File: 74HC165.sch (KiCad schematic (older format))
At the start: 6 parts, among them J10 Conn_01x04, J9 Conn_01x04, U1 74HC165

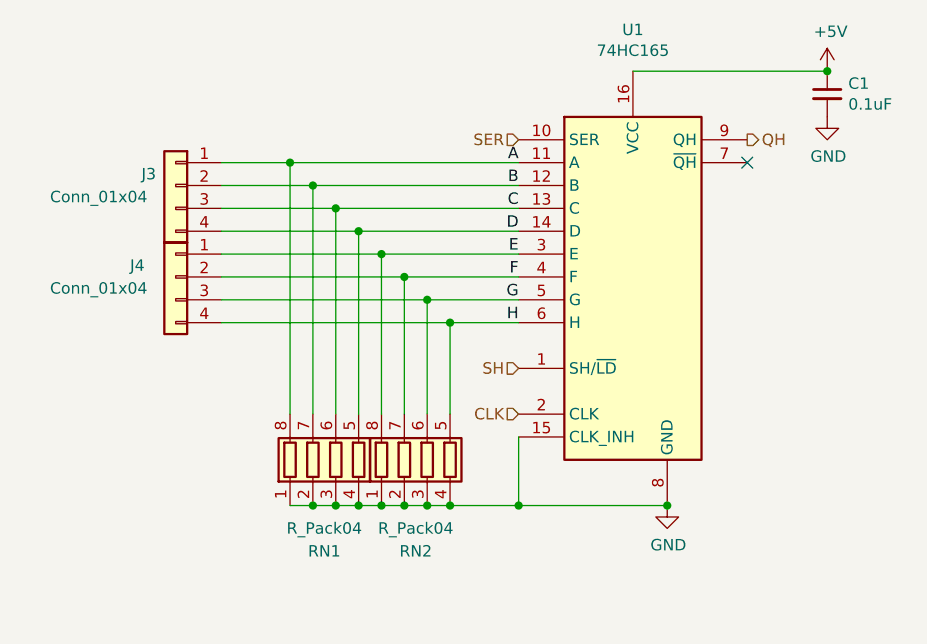
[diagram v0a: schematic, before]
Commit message: Add GND to each header, remove daisy chain
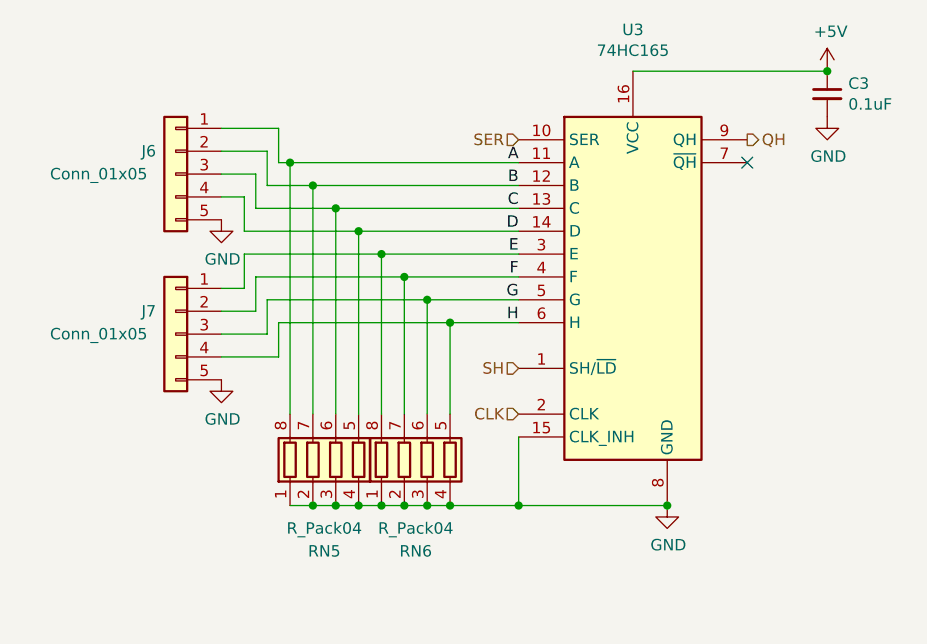
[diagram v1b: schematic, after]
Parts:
- removed J10, J9: Conn_01x04, Connector_JST:JST_XH_B4B-XH-AM_1x04_P2.50mm_Vertical, symbol Connector_Generic:Conn_01x04
- added J2, J3: Conn_01x05, Connector_JST:JST_XH_B5B-XH-A_1x05_P2.50mm_Vertical, symbol Connector_Generic:Conn_01x05
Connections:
- net A: now also J2.1 (Pin_1)
- net B: now also J2.2 (Pin_2)
- net C: now also J2.3 (Pin_3)
- net D: now also J2.4 (Pin_4)
- net E: now also J3.1 (Pin_1)
- net F: now also J3.2 (Pin_2)
- net G: now also J3.3 (Pin_3)
- net GND: now also J2.5 (Pin_5), J3.5 (Pin_5)
- net H: now also J3.4 (Pin_4)
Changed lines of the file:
@@
 $Descr A4 11693 8268
 encoding utf-8
-Sheet 2 5
+Sheet 4 5
 Title ""
 Date "%%date%%"
@@
 AR Path="/61DDC3C8/61DD4B9D" Ref="U3"  Part="1"
 AR Path="/61DDC5F2/61DD4B9D" Ref="U4"  Part="1"
-F 0 "U1" H 3350 2931 50  0000 C CNN
+F 0 "U3" H 3350 2931 50  0000 C CNN
 F 1 "74HC165" H 3350 2840 50  0000 C CNN
 F 2 "Package_SO:TSSOP-16_4.4x5mm_P0.65mm" H 3350 1850 50  0001 C CNN
@@
 AR Path="/61DDC3C8/61DD4BA3" Ref="C3"  Part="1"
 AR Path="/61DDC5F2/61DD4BA3" Ref="C4"  Part="1"
-F 0 "C1" H 4292 1096 50  0000 L CNN
+F 0 "C3" H 4292 1096 50  0000 L CNN
 F 1 "0.1uF" H 4292 1005 50  0000 L CNN
 F 2 "Capacitor_SMD:C_0805_2012Metric" H 4200 1050 50  0001 C CNN
@@
 	2850 2850 3500 2850
 Wire Wire Line
-	1550 1950 2450 1950
-Wire Wire Line
-	1550 2050 2550 2050
-Wire Wire Line
 	2550 2450 2550 2050
-Connection ~ 2550 2050
 Wire Wire Line
 	2550 2050 2850 2050
 Wire Wire Line
-	1550 1350 1850 1350
-Wire Wire Line
-	1550 1450 1950 1450
-Wire Wire Line
-	1550 1550 2050 1550
-Wire Wire Line
-	1550 1650 2150 1650
-Wire Wire Line
-	1550 1750 2250 1750
-Wire Wire Line
-	1550 1850 2350 1850
-Wire Wire Line
 	2450 2450 2450 1950
-Connection ~ 2450 1950
 Wire Wire Line
 	2450 1950 2850 1950
 Wire Wire Line
 	2350 2450 2350 1850
-Connection ~ 2350 1850
 Wire Wire Line
 	2350 1850 2850 1850
 Wire Wire Line
 	2250 2450 2250 1750
-Connection ~ 2250 1750
 Wire Wire Line
 	2250 1750 2850 1750
 Wire Wire Line
 	2150 2450 2150 1650
-Connection ~ 2150 1650
 Wire Wire Line
 	2150 1650 2850 1650
 Wire Wire Line
 	2050 2450 2050 1550
-Connection ~ 2050 1550
 Wire Wire Line
 	2050 1550 2850 1550
 Wire Wire Line
 	1950 2450 1950 1450
-Connection ~ 1950 1450
 Wire Wire Line
 	1950 1450 2850 1450
 Wire Wire Line
 	1850 2450 1850 1350
-Connection ~ 1850 1350
 Wire Wire Line
 	1850 1350 2850 1350
@@
 AR Path="/61DD4BEE" Ref="#PWR?"  Part="1"
 AR Path="/61DCCBDC/61DD4BEE" Ref="#PWR07"  Part="1"
-AR Path="/61DDC172/61DD4BEE" Ref="#PWR010"  Part="1"
-AR Path="/61DDC3C8/61DD4BEE" Ref="#PWR013"  Part="1"
-AR Path="/61DDC5F2/61DD4BEE" Ref="#PWR016"  Part="1"
-F 0 "#PWR07" H 3500 2600 50  0001 C CNN
+AR Path="/61DDC172/61DD4BEE" Ref="#PWR012"  Part="1"
+AR Path="/61DDC3C8/61DD4BEE" Ref="#PWR017"  Part="1"
+AR Path="/61DDC5F2/61DD4BEE" Ref="#PWR022"  Part="1"
+F 0 "#PWR017" H 3500 2600 50  0001 C CNN
 F 1 "GND" H 3505 2677 50  0000 C CNN
 F 2 "" H 3500 2850 50  0001 C CNN
@@
 P 4200 950
 AR Path="/61DD4BF6" Ref="#PWR?"  Part="1"
-AR Path="/61DCCBDC/61DD4BF6" Ref="#PWR05"  Part="1"
+AR Path="/61DCCBDC/61DD4BF6" Ref="#PWR03"  Part="1"
 AR Path="/61DDC172/61DD4BF6" Ref="#PWR08"  Part="1"
-AR Path="/61DDC3C8/61DD4BF6" Ref="#PWR011"  Part="1"
-AR Path="/61DDC5F2/61DD4BF6" Ref="#PWR014"  Part="1"
-F 0 "#PWR05" H 4200 800 50  0001 C CNN
+AR Path="/61DDC3C8/61DD4BF6" Ref="#PWR013"  Part="1"
+AR Path="/61DDC5F2/61DD4BF6" Ref="#PWR018"  Part="1"
+F 0 "#PWR013" H 4200 800 50  0001 C CNN
 F 1 "+5V" H 4215 1123 50  0000 C CNN
 F 2 "" H 4200 950 50  0001 C CNN
@@
 P 4200 1150
 AR Path="/61DD4BFD" Ref="#PWR?"  Part="1"
-AR Path="/61DCCBDC/61DD4BFD" Ref="#PWR06"  Part="1"
+AR Path="/61DCCBDC/61DD4BFD" Ref="#PWR04"  Part="1"
 AR Path="/61DDC172/61DD4BFD" Ref="#PWR09"  Part="1"
-AR Path="/61DDC3C8/61DD4BFD" Ref="#PWR012"  Part="1"
-AR Path="/61DDC5F2/61DD4BFD" Ref="#PWR015"  Part="1"
-F 0 "#PWR06" H 4200 900 50  0001 C CNN
+AR Path="/61DDC3C8/61DD4BFD" Ref="#PWR014"  Part="1"
+AR Path="/61DDC5F2/61DD4BFD" Ref="#PWR019"  Part="1"
+F 0 "#PWR014" H 4200 900 50  0001 C CNN
 F 1 "GND" H 4205 977 50  0000 C CNN
 F 2 "" H 4200 1150 50  0001 C CNN
@@
 H
 $Comp
-L Connector_Generic:Conn_01x04 J9
-U 1 1 61DF079D
-P 1350 1450
-AR Path="/61DDC5F2/61DF079D" Ref="J9"  Part="1"
-AR Path="/61DCCBDC/61DF079D" Ref="J3"  Part="1"
-AR Path="/61DDC172/61DF079D" Ref="J5"  Part="1"
-AR Path="/61DDC3C8/61DF079D" Ref="J7"  Part="1"
-F 0 "J3" H 1500 1500 50  0000 R CNN
-F 1 "Conn_01x04" H 1900 1400 50  0000 R CNN
-F 2 "Connector_JST:JST_XH_B4B-XH-AM_1x04_P2.50mm_Vertical" H 1350 1450 50  0001 C CNN
-F 3 "~" H 1350 1450 50  0001 C CNN
-	1    1350 1450
-	-1   0    0    -1
-$EndComp
-$Comp
-L Connector_Generic:Conn_01x04 J10
-U 1 1 61DF3828
-P 1350 1850
-AR Path="/61DDC5F2/61DF3828" Ref="J10"  Part="1"
-AR Path="/61DCCBDC/61DF3828" Ref="J4"  Part="1"
-AR Path="/61DDC172/61DF3828" Ref="J6"  Part="1"
-AR Path="/61DDC3C8/61DF3828" Ref="J8"  Part="1"
-F 0 "J4" H 1550 1900 50  0000 R CNN
-F 1 "Conn_01x04" H 1900 1800 50  0000 R CNN
-F 2 "Connector_JST:JST_XH_B4B-XH-AM_1x04_P2.50mm_Vertical" H 1350 1850 50  0001 C CNN
-F 3 "~" H 1350 1850 50  0001 C CNN
-	1    1350 1850
-	-1   0    0    -1
-$EndComp
-$Comp
 L Device:R_Pack04 RN1
 U 1 1 61DB920B
@@
 AR Path="/61DDC3C8/61DB920B" Ref="RN5"  Part="1"
 AR Path="/61DDC5F2/61DB920B" Ref="RN7"  Part="1"
-F 0 "RN1" H 2000 2250 50  0000 C CNN
+F 0 "RN5" H 2000 2250 50  0000 C CNN
 F 1 "R_Pack04" H 2000 2350 50  0000 C CNN
 F 2 "Resistor_SMD:R_Array_Convex_4x1206" V 2325 2650 50  0001 C CNN
@@
 AR Path="/61DDC3C8/61DBAD50" Ref="RN6"  Part="1"
 AR Path="/61DDC5F2/61DBAD50" Ref="RN8"  Part="1"
-F 0 "RN2" H 2400 2250 50  0000 C CNN
+F 0 "RN6" H 2400 2250 50  0000 C CNN
 F 1 "R_Pack04" H 2400 2350 50  0000 C CNN
 F 2 "Resistor_SMD:R_Array_Convex_4x1206" V 2725 2650 50  0001 C CNN
@@
 Wire Wire Line
 	2550 2850 2850 2850
+$Comp
+L Connector_Generic:Conn_01x05 J3
+U 1 1 61DCA935
+P 1350 2100
+AR Path="/61DCCBDC/61DCA935" Ref="J3"  Part="1"
+AR Path="/61DDC172/61DCA935" Ref="J5"  Part="1"
+AR Path="/61DDC3C8/61DCA935" Ref="J7"  Part="1"
+AR Path="/61DDC5F2/61DCA935" Ref="J9"  Part="1"
+F 0 "J7" H 1500 2200 50  0000 R CNN
+F 1 "Conn_01x05" H 1900 2100 50  0000 R CNN
+F 2 "Connector_JST:JST_XH_B5B-XH-A_1x05_P2.50mm_Vertical" H 1350 2100 50  0001 C CNN
+F 3 "~" H 1350 2100 50  0001 C CNN
+	1    1350 2100
+	-1   0    0    -1
+$EndComp
+$Comp
+L power:GND #PWR06
+U 1 1 61DCA93B
+P 1550 2300
+AR Path="/61DCCBDC/61DCA93B" Ref="#PWR06"  Part="1"
+AR Path="/61DDC172/61DCA93B" Ref="#PWR011"  Part="1"
+AR Path="/61DDC3C8/61DCA93B" Ref="#PWR016"  Part="1"
+AR Path="/61DDC5F2/61DCA93B" Ref="#PWR021"  Part="1"
+F 0 "#PWR016" H 1550 2050 50  0001 C CNN
+F 1 "GND" H 1555 2127 50  0000 C CNN
+F 2 "" H 1550 2300 50  0001 C CNN
+F 3 "" H 1550 2300 50  0001 C CNN
+	1    1550 2300
+	1    0    0    -1
+$EndComp
+$Comp
+L Connector_Generic:Conn_01x05 J2
+U 1 1 61DCC07D
+P 1350 1400
+AR Path="/61DCCBDC/61DCC07D" Ref="J2"  Part="1"
+AR Path="/61DDC172/61DCC07D" Ref="J4"  Part="1"
+AR Path="/61DDC3C8/61DCC07D" Ref="J6"  Part="1"
+AR Path="/61DDC5F2/61DCC07D" Ref="J8"  Part="1"
+F 0 "J6" H 1500 1500 50  0000 R CNN
+F 1 "Conn_01x05" H 1900 1400 50  0000 R CNN
+F 2 "Connector_JST:JST_XH_B5B-XH-A_1x05_P2.50mm_Vertical" H 1350 1400 50  0001 C CNN
+F 3 "~" H 1350 1400 50  0001 C CNN
+	1    1350 1400
+	-1   0    0    -1
+$EndComp
+$Comp
+L power:GND #PWR05
+U 1 1 61DCC083
+P 1550 1600
+AR Path="/61DCCBDC/61DCC083" Ref="#PWR05"  Part="1"
+AR Path="/61DDC172/61DCC083" Ref="#PWR010"  Part="1"
+AR Path="/61DDC3C8/61DCC083" Ref="#PWR015"  Part="1"
+AR Path="/61DDC5F2/61DCC083" Ref="#PWR020"  Part="1"
+F 0 "#PWR015" H 1550 1350 50  0001 C CNN
+F 1 "GND" H 1555 1427 50  0000 C CNN
+F 2 "" H 1550 1600 50  0001 C CNN
+F 3 "" H 1550 1600 50  0001 C CNN
+	1    1550 1600
+	1    0    0    -1
+$EndComp
+Wire Wire Line
+	2150 1650 1650 1650
+Wire Wire Line
+	1650 1650 1650 1500
+Wire Wire Line
+	1650 1500 1550 1500
+Connection ~ 2150 1650
+Wire Wire Line
+	2050 1550 1700 1550
+Wire Wire Line
+	1700 1550 1700 1400
+Wire Wire Line
+	1700 1400 1550 1400
+Connection ~ 2050 1550
+Wire Wire Line
+	1950 1450 1750 1450
+Wire Wire Line
+	1750 1450 1750 1300
+Wire Wire Line
+	1750 1300 1550 1300
+Connection ~ 1950 1450
+Wire Wire Line
+	1850 1350 1800 1350
+Wire Wire Line
+	1800 1350 1800 1200
+Wire Wire Line
+	1800 1200 1550 1200
+Connection ~ 1850 1350
+Wire Wire Line
+	2250 1750 1650 1750
+Wire Wire Line
+	1650 1750 1650 1900
+Wire Wire Line
+	1650 1900 1550 1900
+Connection ~ 2250 1750
+Wire Wire Line
+	2350 1850 1700 1850
+Wire Wire Line
+	1700 1850 1700 2000
+Wire Wire Line
+	1700 2000 1550 2000
+Connection ~ 2350 1850
+Wire Wire Line
+	2450 1950 1750 1950
+Wire Wire Line
+	1750 1950 1750 2100
+Wire Wire Line
+	1750 2100 1550 2100
+Connection ~ 2450 1950
+Wire Wire Line
+	2550 2050 1800 2050
+Wire Wire Line
+	1800 2050 1800 2200
+Wire Wire Line
+	1800 2200 1550 2200
+Connection ~ 2550 2050
 $EndSCHEMATC

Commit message: Switch to footprints available at JLCPCB
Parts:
- C1: value 0.1uF -> 100nF; JLC (none) -> 0805; LCSC (none) -> C49678
- RN1, RN2: footprint Resistor_SMD:R_Array_Convex_4x1206 -> Resistor_SMD:R_Array_Convex_4x0603; JLC (none) -> 0603_x4; LCSC (none) -> C29718
- U1: footprint Package_SO:TSSOP-16_4.4x5mm_P0.65mm -> Package_SO:SOIC-16_3.9x9.9mm_P1.27mm; JLC (none) -> SOIC-16_3.9x9.9x1.27P; LCSC (none) -> C5613
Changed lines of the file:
@@
 $Descr A4 11693 8268
 encoding utf-8
-Sheet 4 5
+Sheet 3 5
 Title ""
 Date "%%date%%"
@@
 AR Path="/61DDC3C8/61DD4B9D" Ref="U3"  Part="1"
 AR Path="/61DDC5F2/61DD4B9D" Ref="U4"  Part="1"
-F 0 "U3" H 3350 2931 50  0000 C CNN
+F 0 "U2" H 3350 2931 50  0000 C CNN
 F 1 "74HC165" H 3350 2840 50  0000 C CNN
-F 2 "Package_SO:TSSOP-16_4.4x5mm_P0.65mm" H 3350 1850 50  0001 C CNN
+F 2 "Package_SO:SOIC-16_3.9x9.9mm_P1.27mm" H 3350 1850 50  0001 C CNN
 F 3 "https://assets.nexperia.com/documents/data-sheet/74HC_HCT165.pdf" H 3350 1850 50  0001 C CNN
+F 4 "SOIC-16_3.9x9.9x1.27P" H 3350 1850 50  0001 C CNN "JLC"
+F 5 "C5613" H 3350 1850 50  0001 C CNN "LCSC"
 	1    3350 1850
 	1    0    0    -1
@@
 AR Path="/61DDC3C8/61DD4BA3" Ref="C3"  Part="1"
 AR Path="/61DDC5F2/61DD4BA3" Ref="C4"  Part="1"
-F 0 "C3" H 4292 1096 50  0000 L CNN
-F 1 "0.1uF" H 4292 1005 50  0000 L CNN
+F 0 "C2" H 4292 1096 50  0000 L CNN
+F 1 "100nF" H 4292 1005 50  0000 L CNN
 F 2 "Capacitor_SMD:C_0805_2012Metric" H 4200 1050 50  0001 C CNN
 F 3 "~" H 4200 1050 50  0001 C CNN
+F 4 "0805" H 4200 1050 50  0001 C CNN "JLC"
+F 5 "C49678" H 4200 1050 50  0001 C CNN "LCSC"
 	1    4200 1050
 	1    0    0    -1
@@
 AR Path="/61DDC3C8/61DD4BEE" Ref="#PWR017"  Part="1"
 AR Path="/61DDC5F2/61DD4BEE" Ref="#PWR022"  Part="1"
-F 0 "#PWR017" H 3500 2600 50  0001 C CNN
+F 0 "#PWR012" H 3500 2600 50  0001 C CNN
 F 1 "GND" H 3505 2677 50  0000 C CNN
 F 2 "" H 3500 2850 50  0001 C CNN
@@
 AR Path="/61DDC3C8/61DD4BF6" Ref="#PWR013"  Part="1"
 AR Path="/61DDC5F2/61DD4BF6" Ref="#PWR018"  Part="1"
-F 0 "#PWR013" H 4200 800 50  0001 C CNN
+F 0 "#PWR08" H 4200 800 50  0001 C CNN
 F 1 "+5V" H 4215 1123 50  0000 C CNN
 F 2 "" H 4200 950 50  0001 C CNN
@@
 AR Path="/61DDC3C8/61DD4BFD" Ref="#PWR014"  Part="1"
 AR Path="/61DDC5F2/61DD4BFD" Ref="#PWR019"  Part="1"
-F 0 "#PWR014" H 4200 900 50  0001 C CNN
+F 0 "#PWR09" H 4200 900 50  0001 C CNN
 F 1 "GND" H 4205 977 50  0000 C CNN
 F 2 "" H 4200 1150 50  0001 C CNN
@@
 AR Path="/61DDC3C8/61DB920B" Ref="RN5"  Part="1"
 AR Path="/61DDC5F2/61DB920B" Ref="RN7"  Part="1"
-F 0 "RN5" H 2000 2250 50  0000 C CNN
+F 0 "RN3" H 2000 2250 50  0000 C CNN
 F 1 "R_Pack04" H 2000 2350 50  0000 C CNN
-F 2 "Resistor_SMD:R_Array_Convex_4x1206" V 2325 2650 50  0001 C CNN
+F 2 "Resistor_SMD:R_Array_Convex_4x0603" V 2325 2650 50  0001 C CNN
 F 3 "~" H 2050 2650 50  0001 C CNN
+F 4 "0603_x4" H 2050 2650 50  0001 C CNN "JLC"
+F 5 "C29718" H 2050 2650 50  0001 C CNN "LCSC"
 	1    2050 2650
 	1    0    0    -1
@@
 AR Path="/61DDC3C8/61DBAD50" Ref="RN6"  Part="1"
 AR Path="/61DDC5F2/61DBAD50" Ref="RN8"  Part="1"
-F 0 "RN6" H 2400 2250 50  0000 C CNN
+F 0 "RN4" H 2400 2250 50  0000 C CNN
 F 1 "R_Pack04" H 2400 2350 50  0000 C CNN
-F 2 "Resistor_SMD:R_Array_Convex_4x1206" V 2725 2650 50  0001 C CNN
+F 2 "Resistor_SMD:R_Array_Convex_4x0603" V 2725 2650 50  0001 C CNN
 F 3 "~" H 2450 2650 50  0001 C CNN
+F 4 "0603_x4" H 2450 2650 50  0001 C CNN "JLC"
+F 5 "C29718" H 2450 2650 50  0001 C CNN "LCSC"
 	1    2450 2650
 	1    0    0    -1
@@
 AR Path="/61DDC3C8/61DCA935" Ref="J7"  Part="1"
 AR Path="/61DDC5F2/61DCA935" Ref="J9"  Part="1"
-F 0 "J7" H 1500 2200 50  0000 R CNN
+F 0 "J5" H 1500 2200 50  0000 R CNN
 F 1 "Conn_01x05" H 1900 2100 50  0000 R CNN
 F 2 "Connector_JST:JST_XH_B5B-XH-A_1x05_P2.50mm_Vertical" H 1350 2100 50  0001 C CNN
@@
 AR Path="/61DDC3C8/61DCA93B" Ref="#PWR016"  Part="1"
 AR Path="/61DDC5F2/61DCA93B" Ref="#PWR021"  Part="1"
-F 0 "#PWR016" H 1550 2050 50  0001 C CNN
+F 0 "#PWR011" H 1550 2050 50  0001 C CNN
 F 1 "GND" H 1555 2127 50  0000 C CNN
 F 2 "" H 1550 2300 50  0001 C CNN
@@
 AR Path="/61DDC3C8/61DCC07D" Ref="J6"  Part="1"
 AR Path="/61DDC5F2/61DCC07D" Ref="J8"  Part="1"
-F 0 "J6" H 1500 1500 50  0000 R CNN
+F 0 "J4" H 1500 1500 50  0000 R CNN
 F 1 "Conn_01x05" H 1900 1400 50  0000 R CNN
 F 2 "Connector_JST:JST_XH_B5B-XH-A_1x05_P2.50mm_Vertical" H 1350 1400 50  0001 C CNN
@@
 AR Path="/61DDC3C8/61DCC083" Ref="#PWR015"  Part="1"
 AR Path="/61DDC5F2/61DCC083" Ref="#PWR020"  Part="1"
-F 0 "#PWR015" H 1550 1350 50  0001 C CNN
+F 0 "#PWR010" H 1550 1350 50  0001 C CNN
 F 1 "GND" H 1555 1427 50  0000 C CNN
 F 2 "" H 1550 1600 50  0001 C CNN

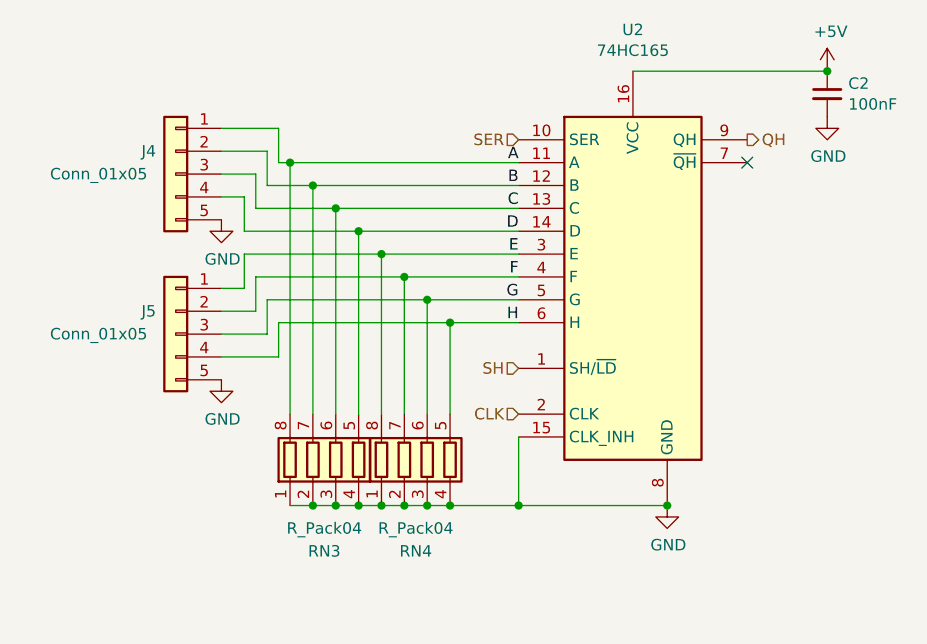
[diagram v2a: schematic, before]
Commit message: Fix resistors, add tooling holes, add test points
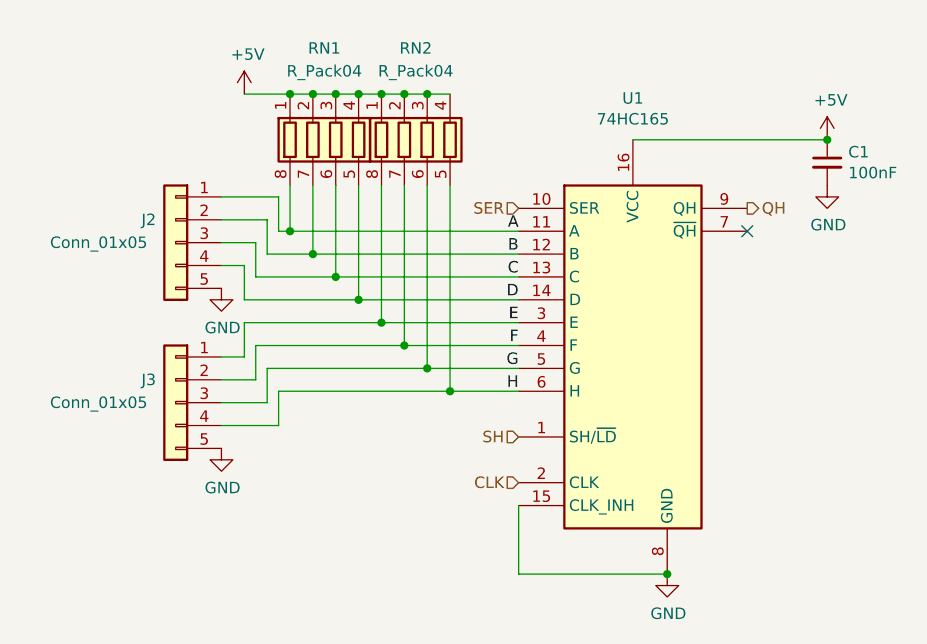
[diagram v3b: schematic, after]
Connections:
- net +5V: now also RN1.1 (R1.1), RN1.2 (R2.1), RN1.3 (R3.1), RN1.4 (R4.1), RN2.1 (R1.1), RN2.2 (R2.1), RN2.3 (R3.1), RN2.4 (R4.1)
- net GND: no longer RN1.1 (R1.1), RN1.2 (R2.1), RN1.3 (R3.1), RN1.4 (R4.1), RN2.1 (R1.1), RN2.2 (R2.1), RN2.3 (R3.1), RN2.4 (R4.1)
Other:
- moved on the sheet: C1, J2, J3, RN1, RN2, U1
